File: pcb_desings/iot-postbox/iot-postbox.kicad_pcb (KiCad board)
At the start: 2 copper layers, 31 x 43.6 mm, 39 parts, among them J1 Switch_1, J2 Switch_2, J3 PowerIn, J4 USB_B_Micro, J5 Battery, J6 Battery, SW1 POWER, U1 ESP-12F, U2 TTL_UART_adapter_iot_postbox, U3 TP4056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

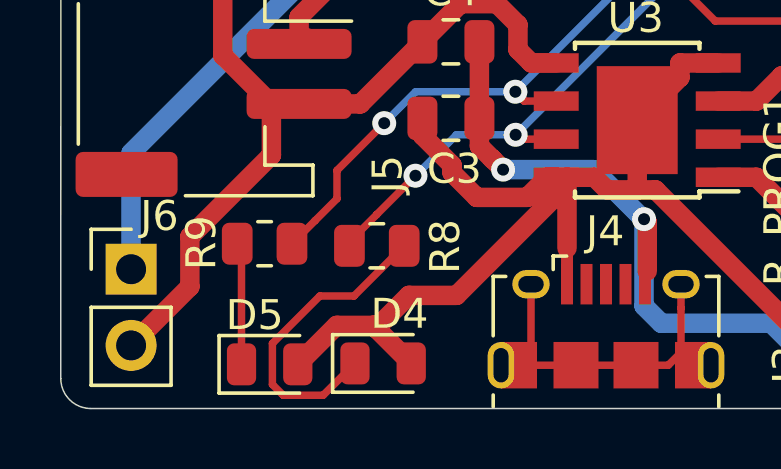
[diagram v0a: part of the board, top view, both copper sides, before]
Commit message: Update some labels for pcb v0.1
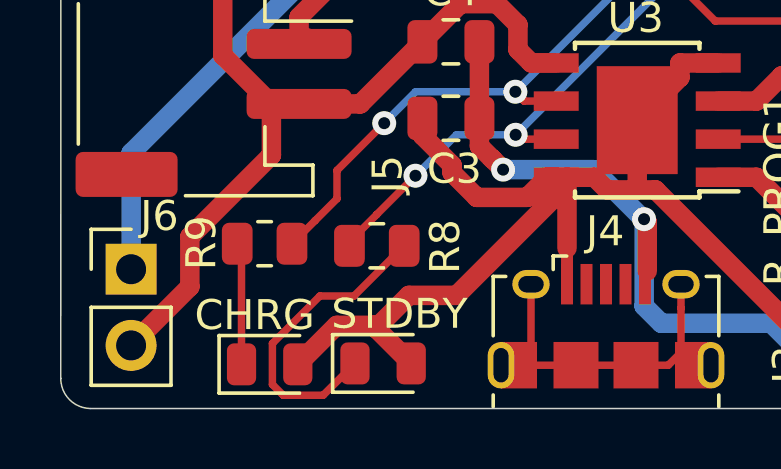
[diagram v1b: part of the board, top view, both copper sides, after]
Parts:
- renumbered D5 to CHRG, D4 to STDBY
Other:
- board text added: "v0.1"
- board text removed: "v.0.0"

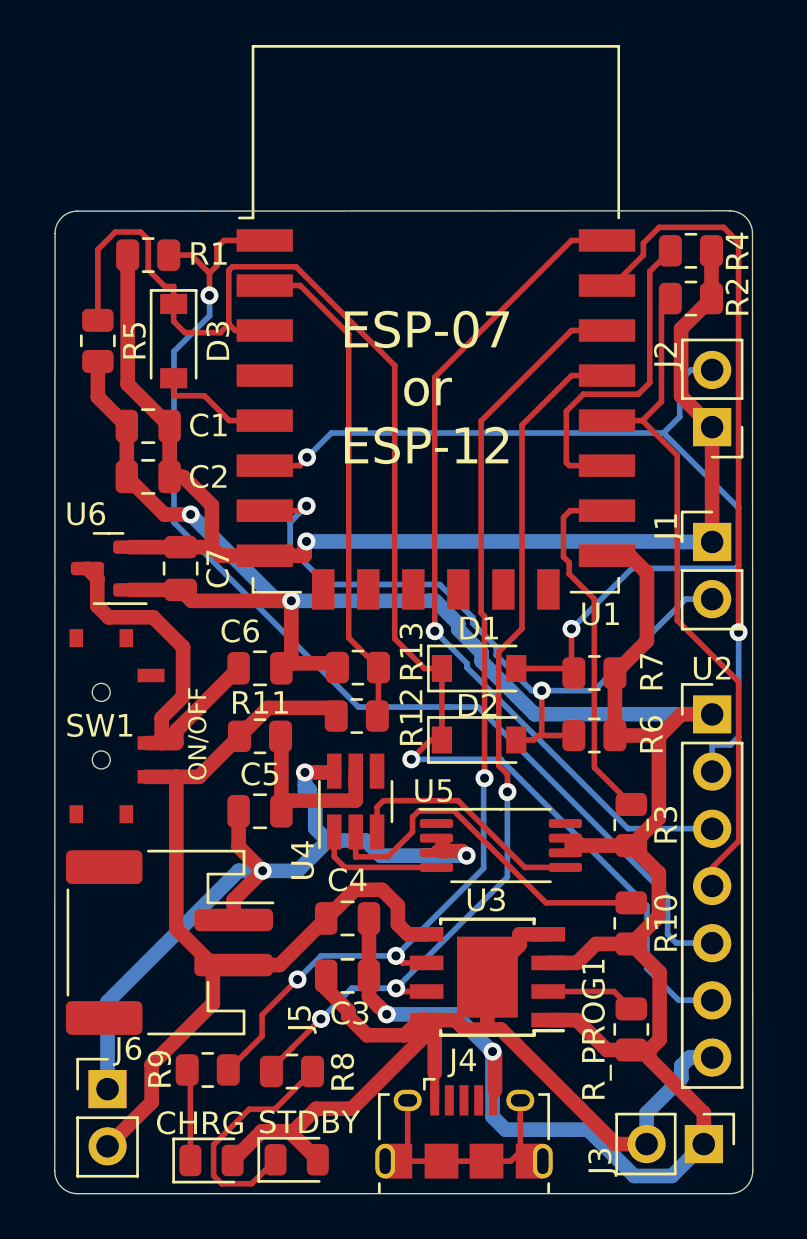
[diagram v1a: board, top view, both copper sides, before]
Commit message: Updated iotpostbox sch to v0.1 and pcb to v0.2. Fixed tp4056 radiator and updated battery adc resistances
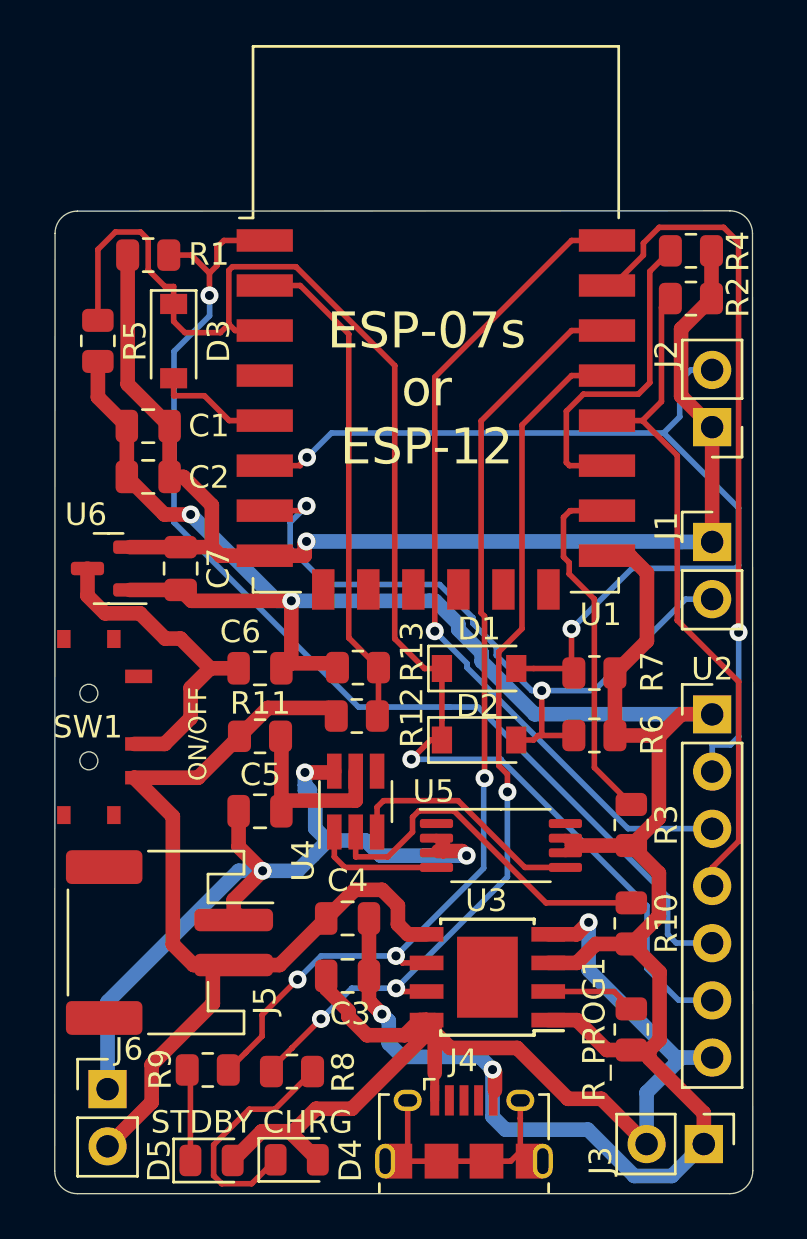
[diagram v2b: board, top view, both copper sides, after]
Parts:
- D4: renamed from STDBY; value LED -> CHRG
- D5: renamed from CHRG; value LED -> STDBY
- R12: value 27K -> 100K
- R13: value 100K -> 30K
- moved SW1 0.55 mm to (101.3, 131.7)
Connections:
- U3 pad 9: IN+ -> (no net)
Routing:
- net IN+: track 47.9 -> 52.3 mm, vias 0 -> 1
- net BAT+: track 41.0 -> 43.8 mm
- net /OUT: track 16.9 -> 14.8 mm
- net IN-: track 123.6 -> 122.9 mm
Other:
- board text added: "ESP-07s or ESP-12"
- board text added: "v0.2"
- board text removed: "ESP-07 or ESP-12"
- board text removed: "v0.1"
